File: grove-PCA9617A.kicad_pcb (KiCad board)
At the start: 2 copper layers, 18.4 x 10.7 mm, 5 parts, among them J1 Grove-I2C-connector, J2 Grove-I2C-connector, U1 PCA9617

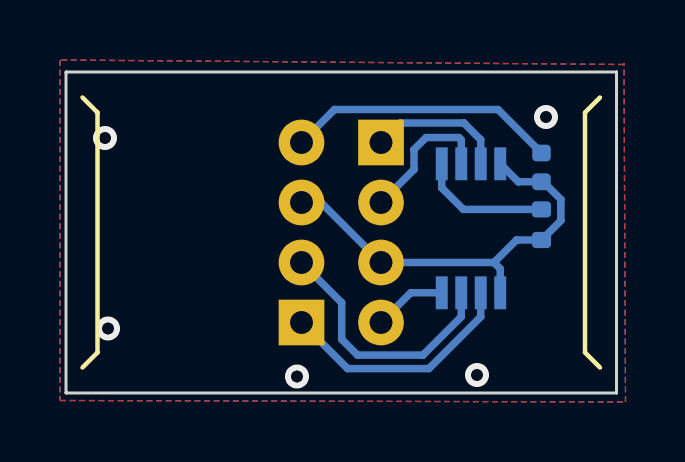
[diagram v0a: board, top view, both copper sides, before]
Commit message: Add pullup resistors
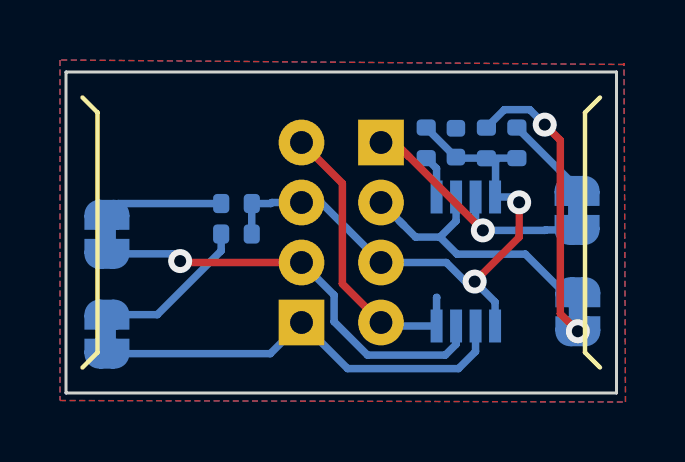
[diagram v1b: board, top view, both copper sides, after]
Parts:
- added JP1: Bridged, Jumper:SolderJumper-2_P1.3mm_Bridged_RoundedPad1.0x1.5mm, B.Cu at (167.6, 60.5)
- added JP2: Bridged, Jumper:SolderJumper-2_P1.3mm_Bridged_RoundedPad1.0x1.5mm, B.Cu at (167.6, 57.2)
- added JP3: Bridged, Jumper:SolderJumper-2_P1.3mm_Bridged_RoundedPad1.0x1.5mm, B.Cu at (183.2, 56.4)
- added JP4: Bridged, Jumper:SolderJumper-2_P1.3mm_Bridged_RoundedPad1.0x1.5mm, B.Cu at (183.3, 59.8)
- added R2: 10k, Resistor_SMD:R_0402_1005Metric, B.Cu at (171.9, 57.2)
- added R3: 10k, Resistor_SMD:R_0402_1005Metric, B.Cu at (171.9, 56.2)
- added R4: 10k, Resistor_SMD:R_0402_1005Metric, B.Cu at (181.2, 54.2)
- added R5: 10k, Resistor_SMD:R_0402_1005Metric, B.Cu at (180.2, 54.2)
- J1, J2: value Grove-I2C-connector -> Grove-I2C
- moved R1 4.71 mm to (178.2, 54.2), turned to -90 degrees
- moved C1 2.97 mm to (179.2, 54.2)
- moved U1 1.12 mm to (179.5, 58.1)
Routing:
- net Net-(JP4-A): track 0.00 -> 9.75 mm, vias 0 -> 2
- net /SCL0: track 8.13 -> 14.5 mm
- net VCC: track 14.4 -> 20.3 mm, vias 0 -> 2
- net /SDA0: track 8.65 -> 14.6 mm, vias 0 -> 1
- net Net-(JP1-A): track 0.00 -> 5.25 mm
- net /SCL1: track 4.63 -> 9.05 mm, vias 0 -> 1
- net Net-(JP2-A): track 0.00 -> 4.40 mm
- net /SDA1: track 4.79 -> 9.11 mm
- net Net-(U1-EN): track 4.42 -> 1.49 mm
- net Net-(JP3-A): track 0.00 -> 2.77 mm
- net GND: track 11.5 -> 10.3 mm, vias 5 -> 0
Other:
- board text added: "I2C Repeater"
- board text added: "PCA9617A for Grove"
- board text added: "Pullup A"
- board text added: "Pullup B"
- board text added: "Rev2024.07"
- board text removed: "PCA9617A for grove"
- board text removed: "Rev2024.06"
